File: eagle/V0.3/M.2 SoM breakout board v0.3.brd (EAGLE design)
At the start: 140 x 120 mm, 165 parts, among them J1 3-PIN SMD, J10 CON_122_SMD_HEADER, J11 WAFER-HY2.0-4PWB, J12 TP_OPEN, J13 SIM-NANO-4FF, J15 CON_122_SMD_HEADER, J16 SIP-2, J18 PARTICLE-STUDIOS_M_SERIES_M.2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, J19 TP_OPEN, J2 DCJ0202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

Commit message: update
  delete based test:
  2 pinholes for jumpers ，GPIO0  is used for IRQ ADC7   is used for RESET  that is no needed
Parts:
- removed J16: SIP-2, particle SZ:SIP-2
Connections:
- net ADC7: no longer J16.1
- net GPIO0: no longer J16.2
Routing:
- net ADC7: track 125.5 -> 55.4 mm
- net VBAT: track 84.8 -> 80.1 mm
- net GPIO0: track 190.6 -> 188.0 mm
- net VUSB-MCU: track 55.8 -> 53.6 mm
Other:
- board text added: "BLUE"
- board text added: "D2"
- board text added: "D3"
- board text added: "D4"
- board text added: "D5"
- board text added: "D6"
- board text added: "D7"
- board text added: "D8"
- board text added: "GREEN"
- board text added: "LI+"
- board text added: "MD"
- board text added: "MI"
- board text added: "MO"
- board text added: "RED"
- board text added: "RESET"
- board text added: "VUSB"
- board text removed: "/RESET"
- board text removed: "B"
- board text removed: "G"
- board text removed: "R"

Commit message: update
update SCH&PCB
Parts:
- removed J8: TP_OPEN, particle SZ:TP_OPEN
- removed JP9: TP_SHORT, particle SZ:TP_SHORT
- removed LED2: BLUE, particle SZ:LED0603
- removed R22: 10K, particle-studios:R0603_P
- removed R32: nc, particle SZ:R-0402S
- added Q1: HSS2333, RedBear:SOT-23
- added R17: 1K, Particle:R0402_B
- added TP1, TP2, TP5, TP8: TPTPEB, particle SZ:TPEB
- R11: value 1K -> 100K
- R18: value nc -> 6.91K; device particle SZ:R-0402S -> particle SZ:R0603
- R74: value nc -> 83.2K; device particle SZ:R-0402S -> particle SZ:R0603
- moved R11 127.8 mm to (-8.10, 105.9), turned to 270 degrees
- moved R18 39.3 mm to (-3.35, 99.3)
- moved R74 39.0 mm to (-3.35, 102.3)
- moved GND 20.4 mm to (-11.7, 82.5)
- moved D17 7.87 mm to (-17.7, 96.1), turned to 270 degrees
- moved MODE 1.70 mm to (92.9, 5.26)
- moved R12 1.70 mm to (94.5, 7.78)
- moved LED1 1.64 mm to (-1.99, 109.3)
- moved R16 1.64 mm to (-1.99, 106.8)
- moved T1 1.46 mm to (-1.77, 104.8), turned to 0 degrees
- moved J21 0.28 mm to (15.6, 106.2), turned to 270 degrees
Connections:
- removed net 5VDC: J6.3, J6.4, J6.@3, J6.@4, J6.P$3, J6.P$4
- removed net N$44: R16.2, T1.2
- removed net N$59: JP9.2, R11.2
- removed net NC: J6.8, J6.@8, J6.P$8
- new net 3V3_AUX: J11.2, J3.8, J4.2, J6.2, J6.@2, J6.P$2, MS1.2, MS1.2', TP30.TP
- net +3V3: no longer J11.2, J3.8, J4.2, J6.2, J6.@2, J6.P$2, MS1.2, MS1.2', TP30.TP
- net GND: now also TP8.1; no longer LED2.2, R22.1
- net GPIO1: now also J6.7, J6.@7, J6.P$7
- net N$13: now also J21.2, TP2.1, TP5.1; no longer R32.1
- net N$14: now also Q1.2, R11.2, T1.2; no longer J8.2, R32.2
- net N$18: now also Q1.3, R16.2; no longer R15.1, S1.3, S1.6
- net N$36: now also Q1.1, R17.2; no longer LED2.1
- net N$57: now also R15.1, R17.1, S1.3, S1.6; no longer J21.2, R22.2
- net PWM3: no longer JP9.1
- net REGN: now also J6.8, J6.@8, J6.P$8, TP1.1; no longer J6.7, J6.@7, J6.P$7
- net TS: no longer J8.1
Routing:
- net 3V3_AUX: track 0.00 -> 220.4 mm, vias 0 -> 24
- net +3V3: track 539.4 -> 354.7 mm, vias 43 -> 14
- net PWM3: track 228.0 -> 192.8 mm, vias 7 -> 5
- net N$57: track 5.89 -> 41.0 mm, vias 0 -> 1
- net REGN: track 41.0 -> 75.9 mm, vias 1 -> 0
- net N$18: track 26.2 -> 2.54 mm, vias 1 -> 0
- net N$13: track 4.01 -> 27.5 mm, vias 1 -> 0
- net GPIO1: track 184.9 -> 205.7 mm
- net 5VDC: track 15.0 -> 0.00 mm
- net TS: track 42.8 -> 33.8 mm, vias 2 -> 0
- net VCC: track 125.3 -> 131.2 mm, vias 36 -> 33
- net N$14: track 1.31 -> 7.11 mm
- net NC: track 4.06 -> 0.00 mm
- net N$45: track 10.9 -> 14.4 mm
- net N$59: track 3.23 -> 0.00 mm
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- added copper zone on layer 1, net 3V3_AUX
- added copper zone on layer 16, net 3V3_AUX
- added copper zone on layer 2, net 3V3_AUX
- removed copper zone on layer 2, net +3V3
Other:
- board text added: "3V3_AUX"
- board text added: "CELLUAR_USB"
- board text added: "EN_AUX"
- board text removed: "ADC7"
- board text removed: "USER LED"

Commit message: update
update PCB&SCH
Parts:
- removed R74: 83.2K, particle SZ:R0603
- added R22: NC, Particle:R0402_B
- added RT1: 6.91K, particle SZ:R0603
- added RT2: 83.2K, particle SZ:R0603
- J11: device M.2 SoM breakout board v0.2-0228:WAFER-HY2.0-4PWB -> M.2 SoM breakout board v0.3:M.2-SOM-BREAKOUT-BOARD-V0.2-0228_WAFER-HY2.0-4PWB
- R18: value 6.91K -> NC; device particle SZ:R0603 -> Particle:R0402_B
- moved R18 10.8 mm to (-2.44, 110.0)
- moved GND15 7.10 mm to (3.68, 65.5)
- moved LED1 1.64 mm to (-2.44, 107.7), turned to 180 degrees
- moved R11 1.22 mm to (-9.32, 106.0)
- moved R17 1.22 mm to (-9.32, 108.2)
- moved Q1 1.22 mm to (-6.73, 106.9)
- moved R16 0.73 mm to (-2.44, 106.3), turned to 180 degrees
- moved TP1 0.61 mm to (-6.41, 99.3)
- moved TP8 0.61 mm to (-6.41, 102.3)
- moved TP2 0.61 mm to (-1.41, 99.3)
- moved TP5 0.61 mm to (-1.41, 102.3)
- moved 3V3 0.36 mm to (11.5, 65.5)
- moved R33 0.20 mm to (5.79, 108.4)
- moved T1 0.13 mm to (-1.89, 104.9), turned to 180 degrees
- moved R30 0.10 mm to (5.79, 107.3)
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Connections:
- removed net N$19 (its old number): LED1.1, R16.1
- new net N$36: LED1.2, Q1.2, R22.2
- new net N$44: J6.3, J6.@3, J6.P$3
- new net N$59: J6.4, J6.@4, J6.P$4
- net GND: now also Q1.3, R17.1, R22.1, RT2.1; no longer LED1.2, R74.1
- net N$13: now also RT1.1, RT2.2; no longer R18.1, R74.2
- net N$14: now also R16.2; no longer Q1.2, R11.2
- net N$18: now also LED1.1, R16.1, R18.1; no longer Q1.3, R16.2
- net N$57: no longer R17.1
- net PWM1: now also J10.7; no longer J10.11
- net PWM2: now also J10.11; no longer J10.7
- net REGN: now also RT1.2; no longer R18.2
- net VIN: now also R11.2, R18.2
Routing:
- net GND: track 254.3 -> 484.9 mm, vias 640 -> 660
- net VIN: track 8.64 -> 34.7 mm, vias 0 -> 8
- net N$57: track 41.0 -> 26.2 mm
- net N$36: track 0.00 -> 7.00 mm
- net N$14: track 7.11 -> 1.83 mm
- net PWM1: track 181.3 -> 185.8 mm
- net N$44: track 0.00 -> 4.06 mm
- net N$59: track 0.00 -> 4.06 mm
- net N$18: track 2.54 -> 5.64 mm
- net PWM2: track 174.5 -> 177.2 mm
- net TX: track 115.7 -> 113.6 mm
- net 3V3_AUX: track 220.4 -> 222.5 mm
- net RX: track 117.5 -> 115.6 mm
- net CS: track 162.4 -> 160.7 mm
- net SOM8: track 111.1 -> 109.9 mm
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- added copper zone on layer 16, net VIN
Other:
- board text added: "20240404"
- board text added: "CELL_USB"
- board text added: "CHG LED"
- board text added: "J22"
- board text added: "RT1"
- board text added: "RT2"
- board text removed: "20240326"
- board text removed: "CELLUAR_USB"

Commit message: Update
Update SCH&PCB
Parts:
- F5: device adafruit:R1206 -> adafruit:1812
- moved JP2 9.68 mm to (46.7, 62.8)
- moved R28 9.67 mm to (46.7, 64.8)
- moved R29 9.57 mm to (50.8, 64.8)
- moved JP3 9.56 mm to (50.8, 62.8)
- moved J12 9.51 mm to (40.7, 62.8)
- moved R24 9.50 mm to (40.7, 64.8)
- moved JP1 9.50 mm to (42.7, 62.8)
- moved J19 9.49 mm to (44.7, 62.8)
- moved J20 9.48 mm to (48.8, 62.8)
- moved R26 9.48 mm to (48.8, 64.8)
- moved R27 9.40 mm to (42.7, 64.8)
- moved R25 9.39 mm to (44.7, 64.8)
- moved R2 6.10 mm to (34.4, 106.5), turned to 180 degrees
- moved R7 5.12 mm to (34.4, 105.5)
- moved R18 3.75 mm to (-4.83, 107.1), turned to 270 degrees
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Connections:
- net !RESET: now also J15.2
- net SOM17: no longer J15.2
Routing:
- net !RESET: track 239.9 -> 273.9 mm, vias 6 -> 8
- net N$45: track 14.4 -> 0.00 mm
- net N$54: track 12.1 -> 24.9 mm
- net N$50: track 13.0 -> 19.7 mm
- net N$49: track 11.2 -> 15.4 mm, vias 0 -> 2
- net N$7: track 12.7 -> 8.63 mm
- net N$11: track 4.06 -> 0.00 mm
- net SOM17: track 101.0 -> 97.1 mm
- net +3V3: track 355.5 -> 358.6 mm, vias 14 -> 13
- net VCC: track 131.2 -> 128.7 mm
- net GND: track 484.9 -> 482.8 mm, vias 660 -> 673
- net N$9: track 3.06 -> 4.88 mm
- net VIN: track 34.7 -> 32.9 mm
- net N$3: track 23.0 -> 24.7 mm
- net VUSB-MCU: track 53.6 -> 55.0 mm
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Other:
- board text removed: "RESET"

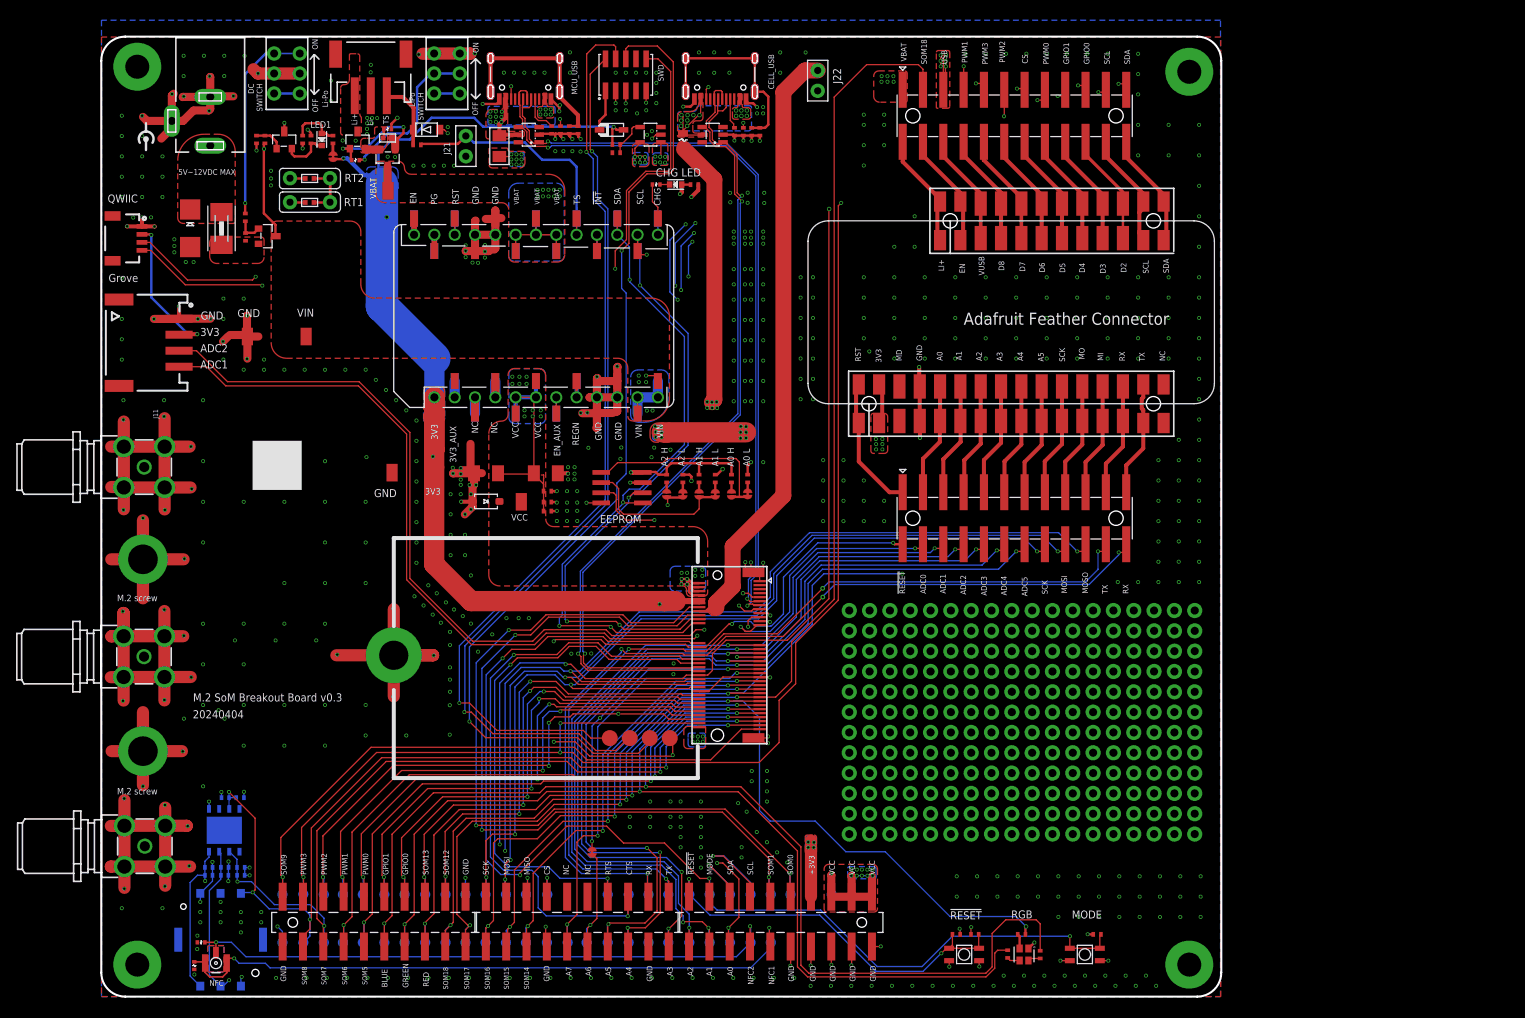
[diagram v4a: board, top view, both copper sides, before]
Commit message: updated v0.3 design
1. Change feather jumpers to smd scratch pads
2. Align proto area with m.2
3. Add 3.3V and GND rail along the proto area
4. LiPo battery pinout change - when we changed from vertical to horizontal, the pinout was flipped. so this is now fixed.
5. Flipped the TX/RX to match the feather pin out
6. Removed EN pin connection to feather
7. Align RGB LED and buttons
8. Align the mounting holes to the corners of the PCB
9. Updated silkscreen and pinout labels on top and bottom
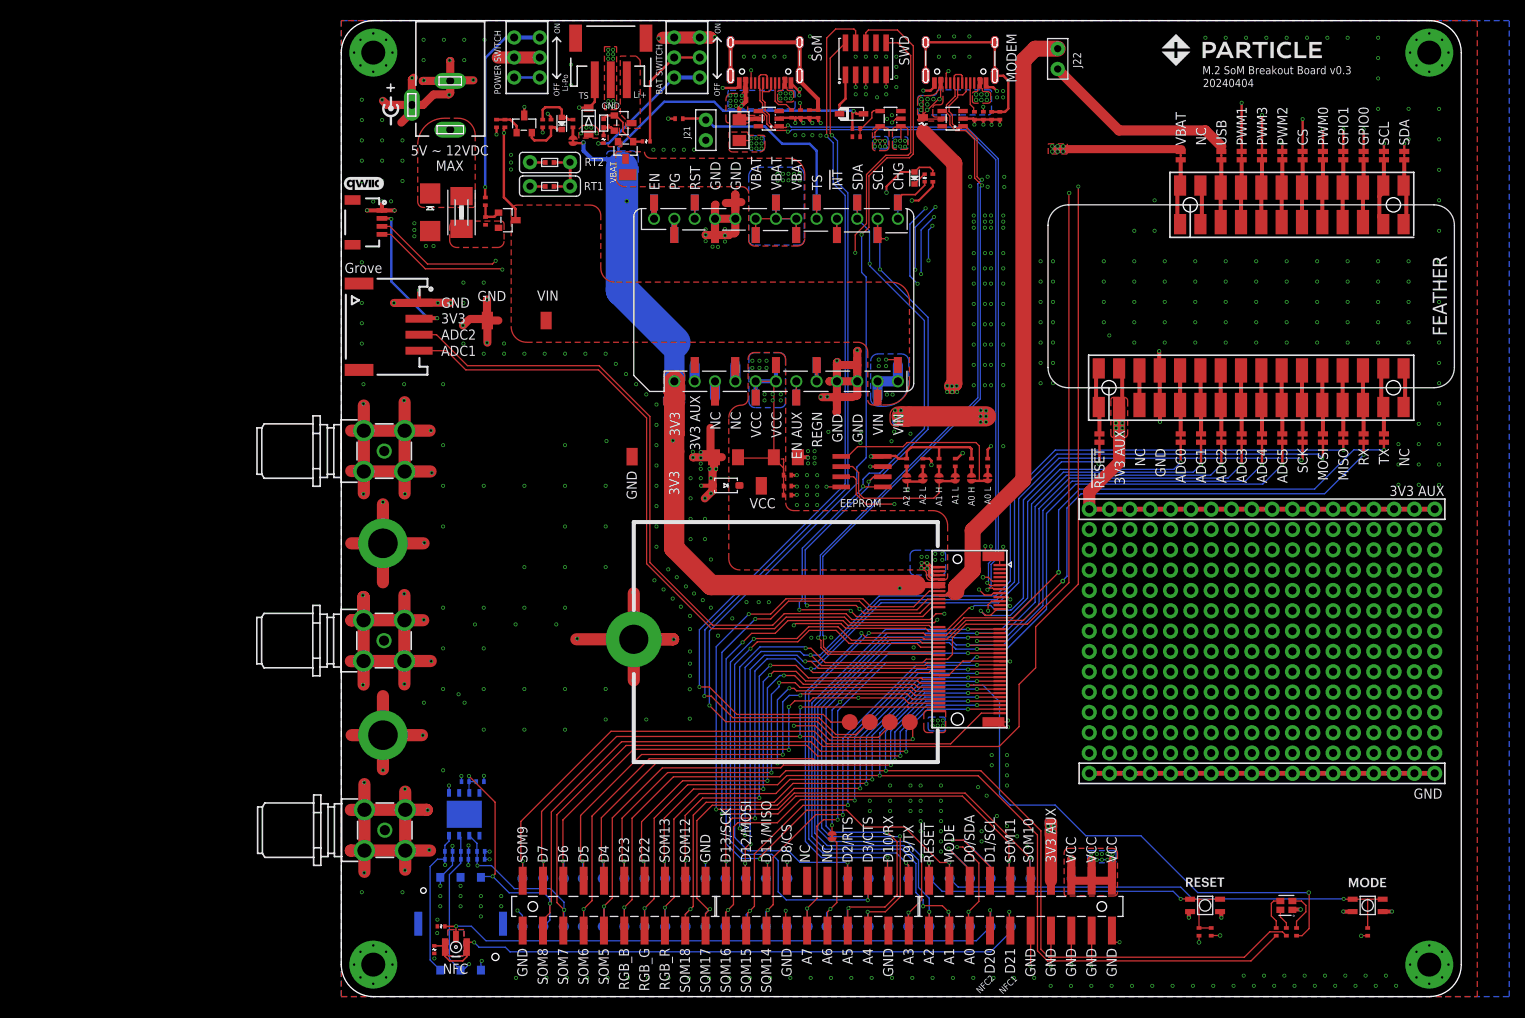
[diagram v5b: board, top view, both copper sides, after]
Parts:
- removed J10, J15: CON_122_SMD_HEADER, Spark:CON_12*2_SMD_HEADER
- added JP10, JP11, JP12, JP13, JP14, JP15, JP16, JP17, JP19, JP20, JP21, JP22, JP23, JP24, JP25, JP26, JP27, JP28, JP5, JP6, JP7, JP8, JP9: JUMPER-SMT_2_NC_TRACE_NO-SILK, SparkFun-Jumpers:SMT-JUMPER_2_NC_TRACE_NO-SILK
- added LOGO2: QWIIC_LOGO_5MM, SparkFun-Aesthetics:QWIIC_5MM
- moved U$6 160.9 mm to (127.3, 118.2), flipped to the bottom
- moved R31 36.4 mm to (38.1, 106.9)
- moved MODE 35.9 mm to (128.3, 11.4)
- moved R20 34.4 mm to (119.4, 8.10), turned to 90 degrees
- moved R12 33.8 mm to (128.3, 8.10), turned to 270 degrees
- moved R19 33.7 mm to (116.9, 8.10), turned to 90 degrees
- moved R13 33.6 mm to (72.9, 102.3), turned to 270 degrees
- moved RGB 33.4 mm to (118.1, 11.4), turned to 0 degrees
- moved Q5 33.2 mm to (35.1, 109.2), turned to 270 degrees
- moved R23 32.9 mm to (42.2, 109.7)
- moved R8 30.9 mm to (118.1, 8.10), turned to 90 degrees
- moved RESET 30.7 mm to (108.0, 11.4)
- moved C1 30.3 mm to (107.2, 8.10), turned to 270 degrees
- moved 3V3 30.2 mm to (41.6, 67.5)
- moved J22 30.1 mm to (89.6, 117.2)
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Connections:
- removed net N$43: J10.4, MS1.27, MS1.27'
- new net EN: MS1.27, MS1.27'
- new net N$223: D4.C, J1.1, R23.2
- new net NC: MS1.16, MS1.16'
- net !RESET: now also JP5.1; no longer J15.2
- net ADC0: now also JP6.1; no longer J15.4
- net ADC1: now also JP7.1; no longer J15.6
- net ADC2: now also JP8.1; no longer J15.8
- net ADC3: now also JP9.1; no longer J15.10
- net ADC4: now also JP10.1; no longer J15.12
- net ADC5: now also JP11.1; no longer J15.14
- net CS: now also JP23.2; no longer J10.13
- net GPIO0: now also JP26.2; no longer J10.19
- net GPIO1: now also JP25.2; no longer J10.17
- net LI+: now also JP17.1; no longer J10.2
- net MISO: now also JP14.1; no longer J15.20
- net MOSI: now also JP13.1; no longer J15.18
- net N$16: now also JP21.1; no longer J10.10
- net N$21: now also JP6.2; no longer J15.3
- net N$23: now also JP7.2; no longer J15.5
- net N$24: now also JP8.2; no longer J15.7
- net N$25: now also JP9.2; no longer J15.9
- net N$26: now also JP10.2; no longer J15.11
- net N$27: now also JP11.2; no longer J15.13
- net N$28: now also JP12.2; no longer J15.15
- net N$29: now also JP13.2; no longer J15.17
- net N$30: now also JP14.2; no longer J15.19
- net N$31: now also JP15.2; no longer J15.21
- net N$32: now also JP16.2; no longer J15.23
- net N$34: now also JP28.1; no longer J10.24
- net N$35: now also JP27.1; no longer J10.22
- net N$37: now also JP26.1; no longer J10.20
- net N$38: now also JP25.1; no longer J10.18
- net N$39: now also JP24.1; no longer J10.16
- net N$40: now also JP23.1; no longer J10.14
- net N$41: now also JP22.1; no longer J10.12
- net N$42: now also JP20.1; no longer J10.8
- net N$46: now also JP5.2; no longer J15.1
- net N$58: now also J1.3; no longer J1.1
- net N$7: now also MS1.3, MS1.3'; no longer D4.C, J1.3, R23.2
- net PWM0: now also JP24.2; no longer J10.15
- net PWM1: now also JP20.2; no longer J10.7
- net PWM2: now also JP22.2; no longer J10.11
- net PWM3: now also JP21.2; no longer J10.9
- net RX: now also JP15.1; no longer J15.24
- net SCK: now also JP12.1; no longer J15.16
- net SCL: now also JP27.2; no longer J10.21
- net SDA: now also JP28.2; no longer J10.23
- net SOM18: no longer J10.3
- net TX: now also JP16.1; no longer J15.22
- net V-USB: now also JP19.1; no longer J10.6
- net VBAT: now also JP17.2; no longer J10.1
- net VUSB-MCU: now also JP19.2; no longer J10.5
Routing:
- net SOM18: track 161.7 -> 66.0 mm
- net 3V3_AUX: track 222.5 -> 280.0 mm, vias 24 -> 42
- net GND: track 482.8 -> 533.7 mm, vias 673 -> 613
- net SOM17: track 97.1 -> 66.4 mm, vias 4 -> 3
- net N$223: track 0.00 -> 17.6 mm, vias 0 -> 2
- net N$43: track 14.6 -> 0.00 mm, vias 0 -> 1
- net TX: track 113.6 -> 126.3 mm
- net ADC1: track 202.2 -> 214.7 mm
- net ADC0: track 79.0 -> 91.4 mm
- net ADC2: track 204.2 -> 216.6 mm
- net ADC3: track 108.6 -> 120.9 mm
- net ADC4: track 111.7 -> 123.9 mm
- net ADC5: track 113.9 -> 126.0 mm
- net SCK: track 126.4 -> 137.0 mm
- net MOSI: track 127.1 -> 137.7 mm
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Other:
- board size 140 x 120 mm -> 140 x 122 mm
- board text added: "3V3 AUX"
- board text added: "5V ~ 12VDC MAX"
- board text added: "BAT SWITCH"
- board text added: "D0/SDA"
- board text added: "D1/SCL"
- board text added: "D10/RX"
- board text added: "D11/MISO"
- board text added: "D12/MOSI"
- board text added: "D13/SCK"
- board text added: "D2/RTS"
- board text added: "D20"
- board text added: "D22"
- board text added: "D23"
- board text added: "D3/CTS"
- board text added: "D8/CS"
- board text added: "D9/TX"
- board text added: "EN AUX"
- board text added: "FEATHER"
- board text added: "MODEM"
- board text added: "POWER SWITCH"
- board text added: "RGB_B"
- board text added: "RGB_G"
- board text added: "RGB_R"
- board text added: "SOM10"
- board text added: "SOM11"
- board text added: "SoM"
- board text removed: "+3V3"
- board text removed: "3V3_AUX"
- board text removed: "5V~12VDC MAX"
- board text removed: "Adafruit Feather Connector"
- board text removed: "BLUE"
- board text removed: "CELL_USB"
- board text removed: "CHG LED"
- board text removed: "CTS"
- board text removed: "D2"
- board text removed: "D3"
- board text removed: "D8"
- board text removed: "DC SWITCH"
- board text removed: "EN_AUX"
- board text removed: "GREEN"
- board text removed: "LI+"
- board text removed: "Li-"
- board text removed: "LiPo SWITCH"
- board text removed: "M.2 screw"
- board text removed: "MCU_USB"
- board text removed: "MD"
- board text removed: "MI"
- board text removed: "MO"
- board text removed: "MOSO"
- board text removed: "QWIIC"
- board text removed: "RED"
- board text removed: "RGB"
- board text removed: "RTS"
- board text removed: "SOM0"
- board text removed: "SOM1"
- board text removed: "VUSB"
